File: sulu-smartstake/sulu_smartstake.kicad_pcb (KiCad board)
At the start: 2 copper layers, 37.4 x 34 mm, 41 parts, among them J1 Conn_01x08, J10 through_hole, J11 through_hole, J12 through_hole, J13 through_hole, J2 Conn_01x02, J3 Conn_02x12_Odd_Even, J4 73391-0060, J5 through_hole, J6 through_hole, J7 through_hole, J8 through_hole, J9 through_hole, M0 NP, M1 NP, M2 NP, M3 NP, M4 NP, M5 NP, M6 NP, M7 NP, U1 TPS62222DDCT, U2 TLV71311PDBV, U3 scum3, U4 SN74LV4051ADR, U5 SN74LV4051ADR

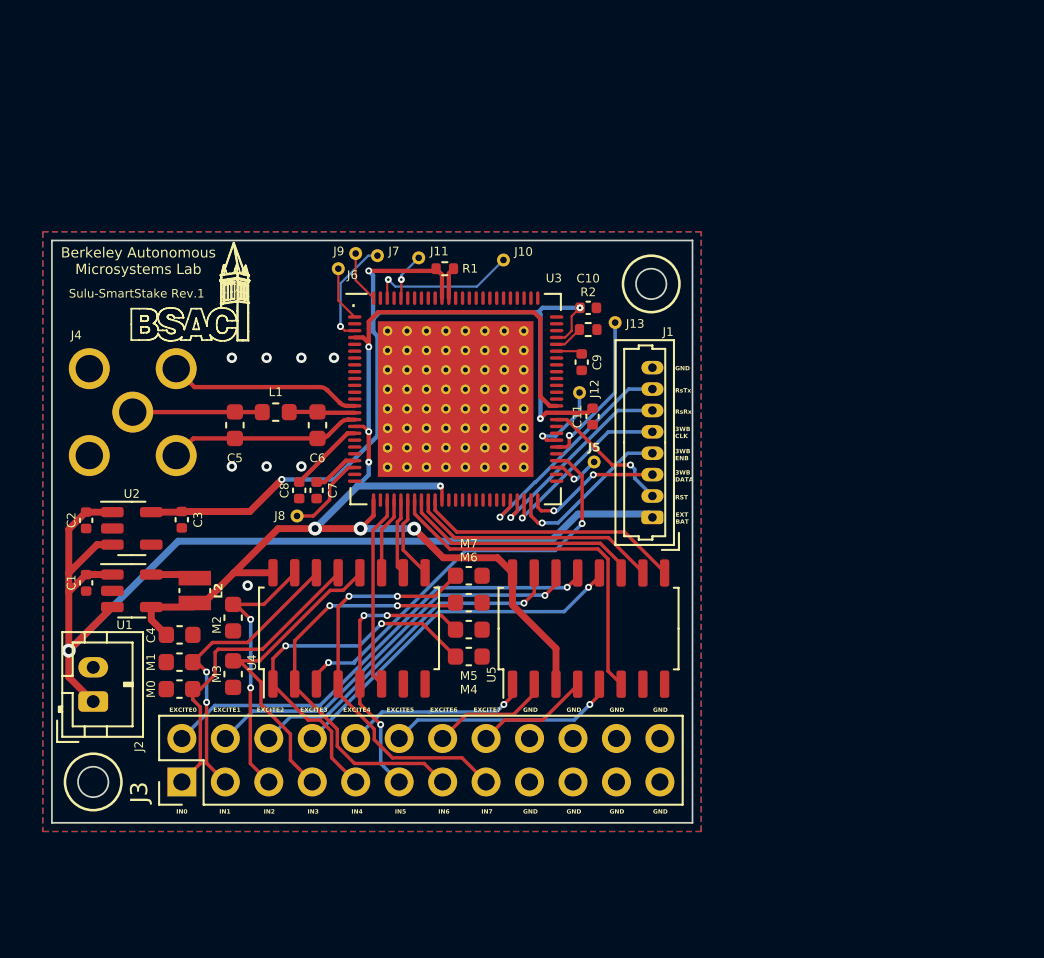
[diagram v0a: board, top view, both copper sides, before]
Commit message: Finalize layout footprint
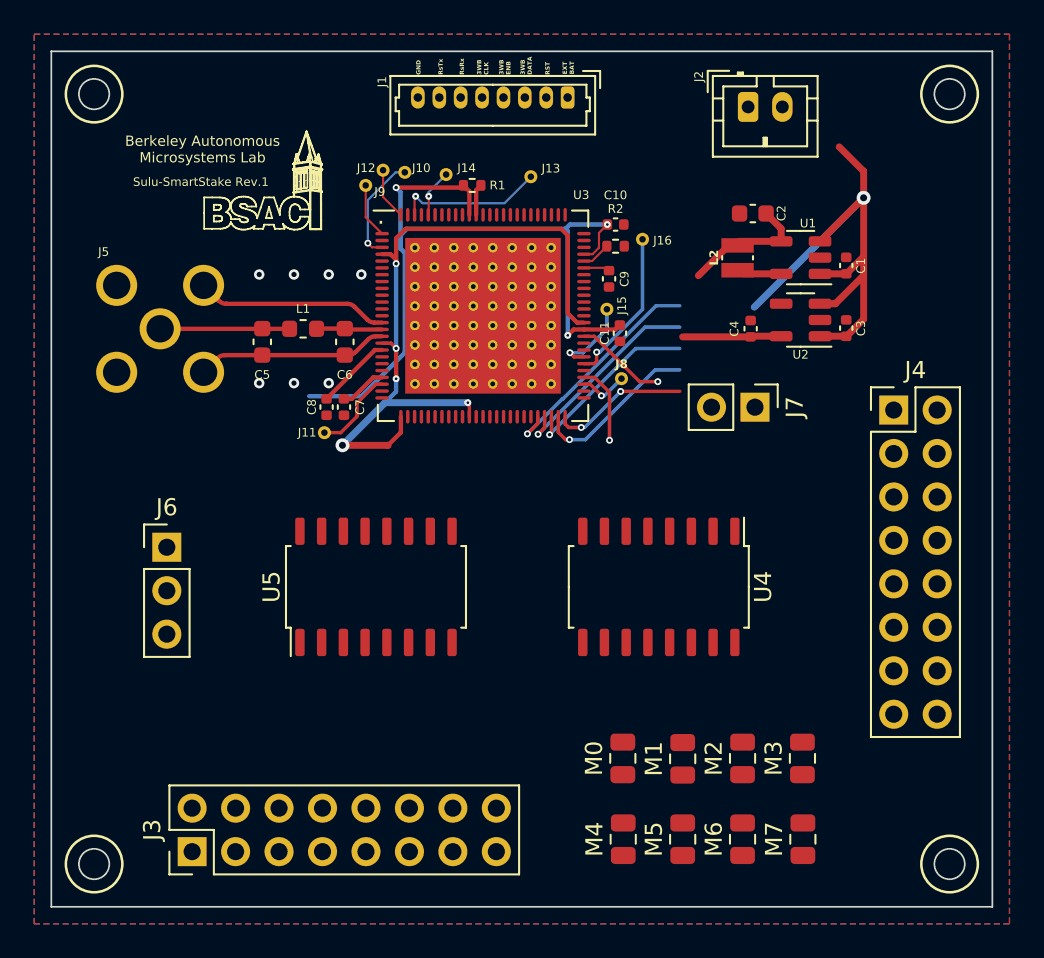
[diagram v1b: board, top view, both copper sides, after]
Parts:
- added J4: Conn_02x08_Odd_Even, Connector_PinHeader_2.54mm:PinHeader_2x08_P2.54mm_Vertical, F.Cu at (129.2, 61.0)
- added J6: Conn_01x03, Connector_PinHeader_2.54mm:PinHeader_1x03_P2.54mm_Vertical, F.Cu at (86.8, 69.0)
- added J7: Conn_01x02, Connector_PinHeader_2.54mm:PinHeader_1x02_P2.54mm_Vertical, F.Cu at (121.1, 60.8)
- J3: value Conn_02x12_Odd_Even -> Conn_02x08_Odd_Even; footprint Connector_PinHeader_2.54mm:PinHeader_2x12_P2.54mm_Vertical -> Connector_PinHeader_2.54mm:PinHeader_2x08_P2.54mm_Vertical
- M0, M1, M2, M3, M4, M5, M6, M7: footprint Capacitor_SMD:C_0603_1608Metric -> Capacitor_SMD:C_0805_2012Metric
- moved J2 51.7 mm to (120.7, 43.2), turned to 0 degrees
- moved C1 48.1 mm to (126.5, 52.5), turned to 90 degrees
- moved C3 45.8 mm to (126.5, 56.2), turned to 90 degrees
- moved U1 43.7 mm to (123.8, 52.1), turned to 180 degrees
- moved C2 41.6 mm to (121.0, 49.5), turned to 0 degrees
- moved U2 40.9 mm to (123.8, 55.7), turned to 180 degrees
- moved L2 37.2 mm to (120.1, 52.1), turned to 90 degrees
- moved C4 35.1 mm to (120.9, 56.2), turned to 90 degrees
- moved M3 33.6 mm to (123.9, 81.3)
- moved M2 30.9 mm to (120.4, 81.3)
- moved M1 29.9 mm to (116.9, 81.3), turned to 90 degrees
- moved M0 26.2 mm to (113.4, 81.3), turned to 90 degrees
- moved J1 25.0 mm to (110.2, 42.7), turned to 180 degrees
- moved M7 24.9 mm to (123.9, 86.0), turned to 90 degrees
- moved M6 21.1 mm to (120.4, 86.0), turned to 90 degrees
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- renumbered C4 to C2, C2 to C3, C3 to C4, J7 to J10, J8 to J11, J9 to J12, J10 to J13, J11 to J14, J12 to J15, J13 to J16, J4 to J5, J5 to J8, J6 to J9
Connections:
- C10 pad 1: +1.1V_REG -> /+1.1V_IN
- C11 pad 1: +1.1V_REG -> /+1.1V_IN
- J3 pad 1: /SENSOR_IN0 -> /SENSOR_EXCITE0
- J3 pad 10: /SENSOR_EXCITE4 -> /SENSOR_IN4
- J3 pad 11: /SENSOR_IN5 -> /SENSOR_EXCITE5
- J3 pad 12: /SENSOR_EXCITE5 -> /SENSOR_IN5
- J3 pad 13: /SENSOR_IN6 -> /SENSOR_EXCITE6
- J3 pad 14: /SENSOR_EXCITE6 -> /SENSOR_IN6
- J3 pad 15: /SENSOR_IN7 -> /SENSOR_EXCITE7
- J3 pad 16: /SENSOR_EXCITE7 -> /SENSOR_IN7
- J3 pad 2: /SENSOR_EXCITE0 -> /SENSOR_IN0
- J3 pad 3: /SENSOR_IN1 -> /SENSOR_EXCITE1
- J3 pad 4: /SENSOR_EXCITE1 -> /SENSOR_IN1
- J3 pad 5: /SENSOR_IN2 -> /SENSOR_EXCITE2
- J3 pad 6: /SENSOR_EXCITE2 -> /SENSOR_IN2
- J3 pad 7: /SENSOR_IN3 -> /SENSOR_EXCITE3
- J3 pad 8: /SENSOR_EXCITE3 -> /SENSOR_IN3
- J3 pad 9: /SENSOR_IN4 -> /SENSOR_EXCITE4
- R1 pad 1: +1.1V_REG -> /+1.1V_IN
- U3 pad 61: +1.1V_REG -> /+1.1V_IN
- U3 pad 72: +1.1V_REG -> /+1.1V_IN
- U3 pad 90: +1.1V_REG -> /+1.1V_IN
- U5 pad 3: +1.8V_REG -> /EXCITE_IN
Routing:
- net +1.1V_REG: track 56.1 -> 5.77 mm, vias 4 -> 0
- net /+1.1V_IN: track 0.00 -> 47.6 mm, vias 0 -> 3
- net +EXT_BAT: track 60.9 -> 32.5 mm
- net /SENSOR_EXCITE0: track 27.3 -> 0.00 mm, vias 1 -> 0
- net +1.8V_REG: track 75.7 -> 50.1 mm, vias 7 -> 5
- net /SENSOR_IN6: track 24.5 -> 0.00 mm, vias 2 -> 0
- net /SENSOR_IN7: track 23.8 -> 0.00 mm, vias 2 -> 0
- net /SENSOR_EXCITE1: track 23.7 -> 0.00 mm, vias 1 -> 0
- net /SENSOR_IN4: track 21.9 -> 0.00 mm, vias 2 -> 0
- net /SENSOR_EXCITE3: track 20.9 -> 0.00 mm, vias 1 -> 0
- net /SCUM_GPIO4: track 20.8 -> 0.00 mm
- net /SENSOR_EXCITE2: track 20.2 -> 0.00 mm, vias 1 -> 0
- net /SENSOR_EXT_IN: track 24.5 -> 4.66 mm, vias 2 -> 1
- net /SENSOR_IN3: track 18.8 -> 0.00 mm
- net /SENSOR_IN0: track 18.2 -> 0.00 mm
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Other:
- board size 37.4 x 34 mm -> 55 x 50 mm
- board text removed: "EXCITE0"
- board text removed: "EXCITE1"
- board text removed: "EXCITE2"
- board text removed: "EXCITE3"
- board text removed: "EXCITE4"
- board text removed: "EXCITE5"
- board text removed: "EXCITE6"
- board text removed: "EXCITE7"
- board text removed: "IN0"
- board text removed: "IN1"
- board text removed: "IN2"
- board text removed: "IN3"
- board text removed: "IN4"
- board text removed: "IN5"
- board text removed: "IN6"
- board text removed: "IN7"

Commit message: Finished layout after review
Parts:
- added J9: through_hole, SCUM:through_hole, F.Cu at (113.5, 63.0)
- moved U4 24.4 mm to (91.1, 71.3), turned to 90 degrees
- moved J6 18.5 mm to (105.2, 68.8)
- moved U5 16.5 mm to (115.5, 71.3)
- moved J7 13.0 mm to (117.7, 48.2), turned to 180 degrees
- moved J17 8.34 mm to (115.8, 59.2)
- moved J14 6.45 mm to (101.6, 46.5)
- moved C4 5.59 mm to (121.0, 50.6)
- moved C3 5.56 mm to (126.6, 50.6)
- moved U2 5.56 mm to (124.0, 50.1)
- moved C2 5.44 mm to (118.0, 54.0), turned to 90 degrees
- moved J16 5.02 mm to (116.7, 57.9)
- moved J11 4.48 mm to (97.1, 49.8)
- moved J8 4.03 mm to (112.0, 63.0)
- moved J2 2.92 mm to (123.6, 43.2)
- moved L2 1.88 mm to (120.3, 53.9)
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- renumbered J9 to J10, J10 to J11, J11 to J12, J12 to J13, J13 to J14, J14 to J15, J15 to J16, J16 to J17
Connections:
- J6 pad 3: /SCUM_GPIO_8 -> /SCUM_GPIO8
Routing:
- net /SENSOR_IN0: track 0.00 -> 80.5 mm, vias 0 -> 1
- net /SENSOR_IN1: track 0.00 -> 75.8 mm, vias 0 -> 3
- net /SENSOR_IN3: track 0.00 -> 72.5 mm, vias 0 -> 1
- net /SENSOR_IN2: track 0.00 -> 71.7 mm, vias 0 -> 3
- net /SENSOR_IN4: track 0.00 -> 62.4 mm, vias 0 -> 1
- net /SENSOR_IN6: track 0.00 -> 56.9 mm, vias 0 -> 1
- net /SENSOR_IN5: track 0.00 -> 54.9 mm, vias 0 -> 3
- net /SENSOR_IN7: track 0.00 -> 52.1 mm, vias 0 -> 1
- net /SENSOR_EXCITE0: track 0.00 -> 45.4 mm, vias 0 -> 2
- net /SENSOR_EXCITE1: track 0.00 -> 41.7 mm, vias 0 -> 2
- net /SENSOR_EXCITE3: track 0.00 -> 38.7 mm, vias 0 -> 2
- net /SENSOR_EXCITE2: track 0.00 -> 38.0 mm, vias 0 -> 2
- net +1.8V_REG: track 50.1 -> 85.5 mm, vias 5 -> 6
- net /SENSOR_EXT_IN: track 4.66 -> 34.9 mm
- net /SENSOR_EXCITE5: track 0.00 -> 26.7 mm
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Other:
- board text added: "1.1V"
- board text added: "1.8V"
- board text added: "EXCITE0"
- board text added: "EXCITE1"
- board text added: "EXCITE2"
- board text added: "EXCITE3"
- board text added: "EXCITE4"
- board text added: "EXCITE5"
- board text added: "EXCITE6"
- board text added: "EXCITE7"
- board text added: "EXCITE_IN"
- board text added: "GPIO8"
- board text added: "IN0"
- board text added: "IN1"
- board text added: "IN2"
- board text added: "IN3"
- board text added: "IN4"
- board text added: "IN5"
- board text added: "IN6"
- board text added: "IN7"

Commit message: Final touches
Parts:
- removed the J8 at (112.0, 63.0)
- removed the J9 at (113.5, 63.0)
- added J5: Conn_02x03_Odd_Even, Connector_PinHeader_2.54mm:PinHeader_2x03_P2.54mm_Vertical, F.Cu at (118.6, 58.0)
- added R3: 0 Ohm, Resistor_SMD:R_0402_1005Metric, F.Cu at (113.2, 56.0)
- moved J15 3.19 mm to (114.8, 60.4)
- moved J16 2.76 mm to (114.3, 61.6)
- moved C1 2.70 mm to (129.3, 53.8)
- moved C2 2.70 mm to (120.6, 53.4)
- moved C3 2.70 mm to (129.3, 50.0)
- moved C4 2.70 mm to (123.7, 50.0)
- moved L2 2.70 mm to (122.9, 53.4)
- moved U1 2.70 mm to (126.6, 53.3)
- moved U2 2.70 mm to (126.6, 49.6)
- moved J7 1.37 mm to (118.1, 49.5)
- moved C9 0.75 mm to (113.0, 52.7), turned to 0 degrees
- moved C11 0.74 mm to (114.1, 55.0)
- moved C10 0.69 mm to (113.0, 49.4)
- moved R2 0.38 mm to (112.9, 51.0)
- moved J2 0.37 mm to (124.0, 43.2)
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- renumbered J11 to J10, J12 to J11, J13 to J12, J14 to J13, J15 to J14, J16 to J15, J17 to J16, J5 to J8, J10 to J9
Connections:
- U3 pad 61: /+1.1V_IN -> Net-(U3-BOOT_SOURCE_SELECT)
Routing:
- net GND: track 22.5 -> 32.2 mm, vias 10 -> 32
- net /SENSOR_EXT_IN: track 34.9 -> 43.5 mm, vias 1 -> 2
- net +1.8V_REG: track 85.5 -> 93.9 mm, vias 6 -> 7
- net /+1.1V_IN: track 31.4 -> 37.6 mm
- net /SENSOR_LDO_OUTPUT: track 4.25 -> 9.77 mm
- net /HARD_RESET: track 23.9 -> 27.2 mm
- net Net-(U3-BOOT_SOURCE_SELECT): track 0.00 -> 1.60 mm
- net +1.1V_REG: track 6.30 -> 7.78 mm
- net +EXT_BAT: track 41.1 -> 42.2 mm
- net Net-(J15-pin): track 5.52 -> 4.68 mm
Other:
- board text added: "SENSOR EXT_IN"
- board text added: "SENSOR LDO_OUT"
